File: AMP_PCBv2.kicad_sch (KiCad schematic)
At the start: 115 parts, among them J1 POWER, J2 EBRAKE, J3 MC, J4 STEERING, J5 OLED Breakout, J6 EBRAKE_BREAKOUT, Q1 Q_NMOS_GDS, Q2 Q_NMOS_GDS, Q3 Q_NMOS_GDS, Q4 Q_NMOS_GDS, U1 Teensy4.0, U10 RFM9x, U2 FT234XD, U3 LM1117-ADJ, U4 LM1117-ADJ, U5 74HC157, U6 74HC157, U7 74HC4060, U8 74HC00, U9 TLV272

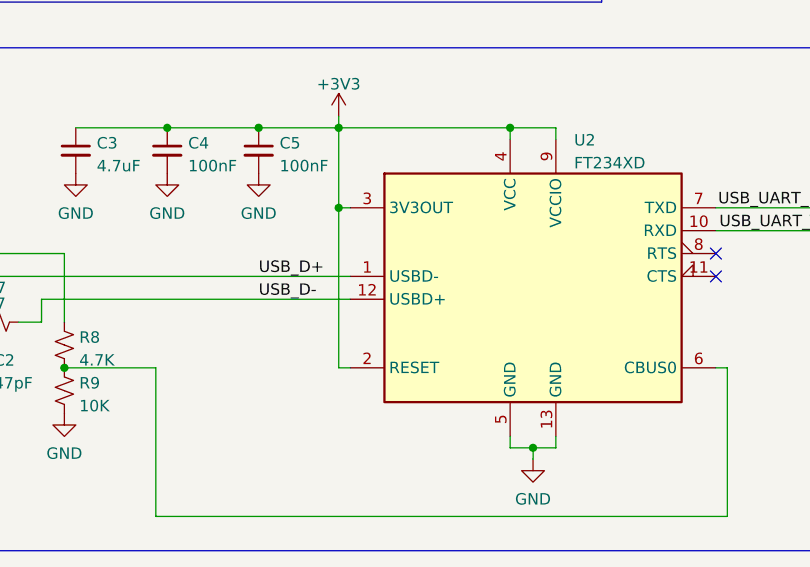
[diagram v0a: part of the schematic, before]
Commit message: Fix D+/D- flipped #4
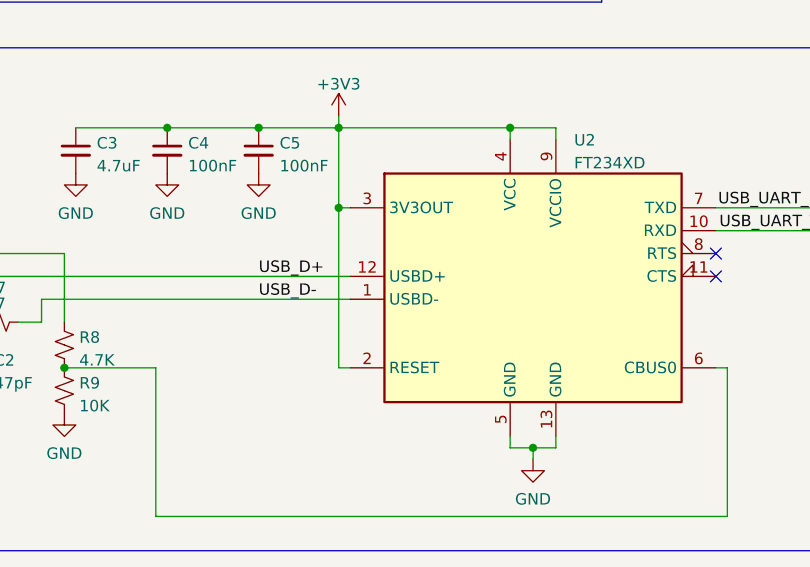
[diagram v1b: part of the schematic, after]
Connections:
- net USB_D+: now also U2.12 (USBD+); no longer U2.1 (USBD-)
- net USB_D-: now also U2.1 (USBD-); no longer U2.12 (USBD+)
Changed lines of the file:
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@@
   (symbol (lib_id "power:+3V3") (at 396.24 194.31 0) (unit 1)
     (in_bom yes) (on_board yes) (fields_autoplaced)
-    (property "Reference" "#PWR?" (id 0) (at 396.24 198.12 0)
+    (property "Reference" "#PWR0109" (id 0) (at 396.24 198.12 0)
       (effects (font (size 1.27 1.27)) hide)
     )
@@
   (symbol (lib_id "power:+3V3") (at 317.5 173.99 0) (unit 1)
     (in_bom yes) (on_board yes) (fields_autoplaced)
-    (property "Reference" "#PWR?" (id 0) (at 317.5 177.8 0)
+    (property "Reference" "#PWR0111" (id 0) (at 317.5 177.8 0)
       (effects (font (size 1.27 1.27)) hide)
     )
@@
       (reference "#PWR0108") (unit 1) (value "GND") (footprint "")
     )
+    (path "/1a40d3a0-f842-45bf-b552-0e18b7a66cde"
+      (reference "#PWR0109") (unit 1) (value "+3V3") (footprint "")
+    )
     (path "/941cc1ef-9c56-488d-859c-ab91af0cdfc0"
       (reference "#PWR0110") (unit 1) (value "GND") (footprint "")
     )
+    (path "/8a2cc60a-ae9d-4eed-bea1-95b3c13b6aaf"
+      (reference "#PWR0111") (unit 1) (value "+3V3") (footprint "")
+    )
     (path "/180d1c7b-1ce2-4e84-81bf-75842d06dc07"
       (reference "#PWR0112") (unit 1) (value "GND") (footprint "")
@@
       (reference "#PWR0181") (unit 1) (value "GND") (footprint "")
     )
-    (path "/1a40d3a0-f842-45bf-b552-0e18b7a66cde"
-      (reference "#PWR?") (unit 1) (value "+3V3") (footprint "")
-    )
-    (path "/8a2cc60a-ae9d-4eed-bea1-95b3c13b6aaf"
-      (reference "#PWR?") (unit 1) (value "+3V3") (footprint "")
-    )
     (path "/16a1e66b-dff9-408a-8eac-84b7497b6789"
